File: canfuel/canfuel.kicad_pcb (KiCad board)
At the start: 2 copper layers, 55 x 45 mm, 0 parts

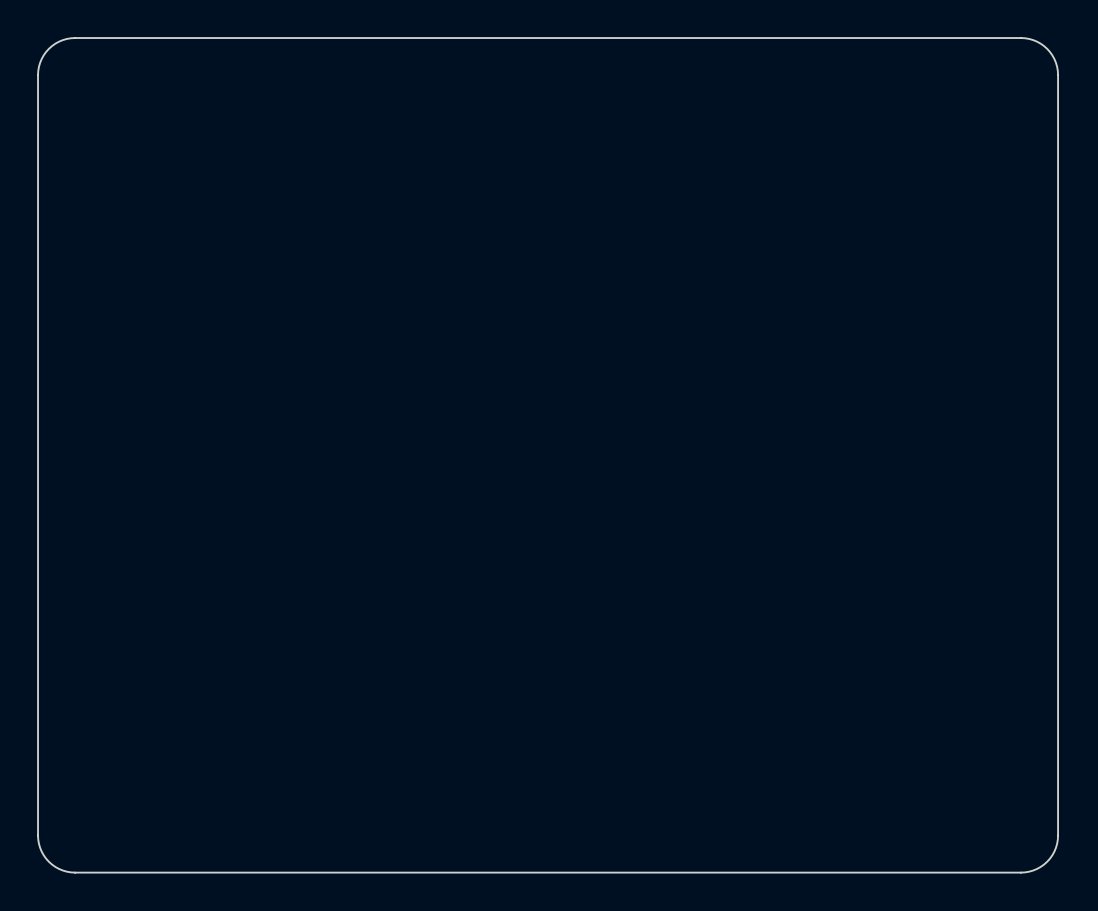
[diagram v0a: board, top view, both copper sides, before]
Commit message: Drop the enclosure and put the mounting holes in
The enclosure has blocked the layout since the project started, on the grounds
that the M3 hole positions were a guess until it was measured and were the one
thing that could force a respin. Closing it by choosing a box turned out to be
the wrong move; closing it by not having one is the right one.

A box was buying nothing here. Everything around the board in the vent is
plastic, so there is no metal to short against. The vent is closed off by a
flap, so there is no airflow, no meaningful dust and no water. The board is
invisible either way. That leaves mechanical retention, and standoffs buy that
better than a box does.

The measurement argued the same way. The space was only ever an estimate - the
MFD15 sits in the way and the depth cannot be measured around it - and the
closest off-the-shelf candidate, a Hammond 1550Q, is 60 x 55 x 30.10 mm against
an estimated 65 x 55 x 30: exactly at the limit on two axes and over on the
third. Its 3 mm die-cast walls would have forced corner notches in the board,
added an isolation and grounding decision that plastic does not, and needed a
slot filed through cast aluminium for the Micro-Fit connectors.

Dropping it inverts the risk. H1-H4 go in at 4 mm from each edge, a 47 x 37 mm
pattern, and because they answer to nothing they stopped being a respin risk
and became cheap insurance: any later mounting scheme is designed around them.
Their references sit on F.Fab rather than F.SilkS, because at 4 mm in from the
edge the silkscreen text overhung the board on the two holes near the top.

Mounting as decided: nylon M3 standoffs, feet on automotive-grade double-sided
tape. Standoffs because the through-hole solder joints must not bear on
anything, VHB-grade tape because a dashboard reaches 50-60 C in summer. Tape
wrapped round the board was considered and rejected - at those temperatures the
adhesive creeps across the board and into the sockets, and it insulates against
metal that 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
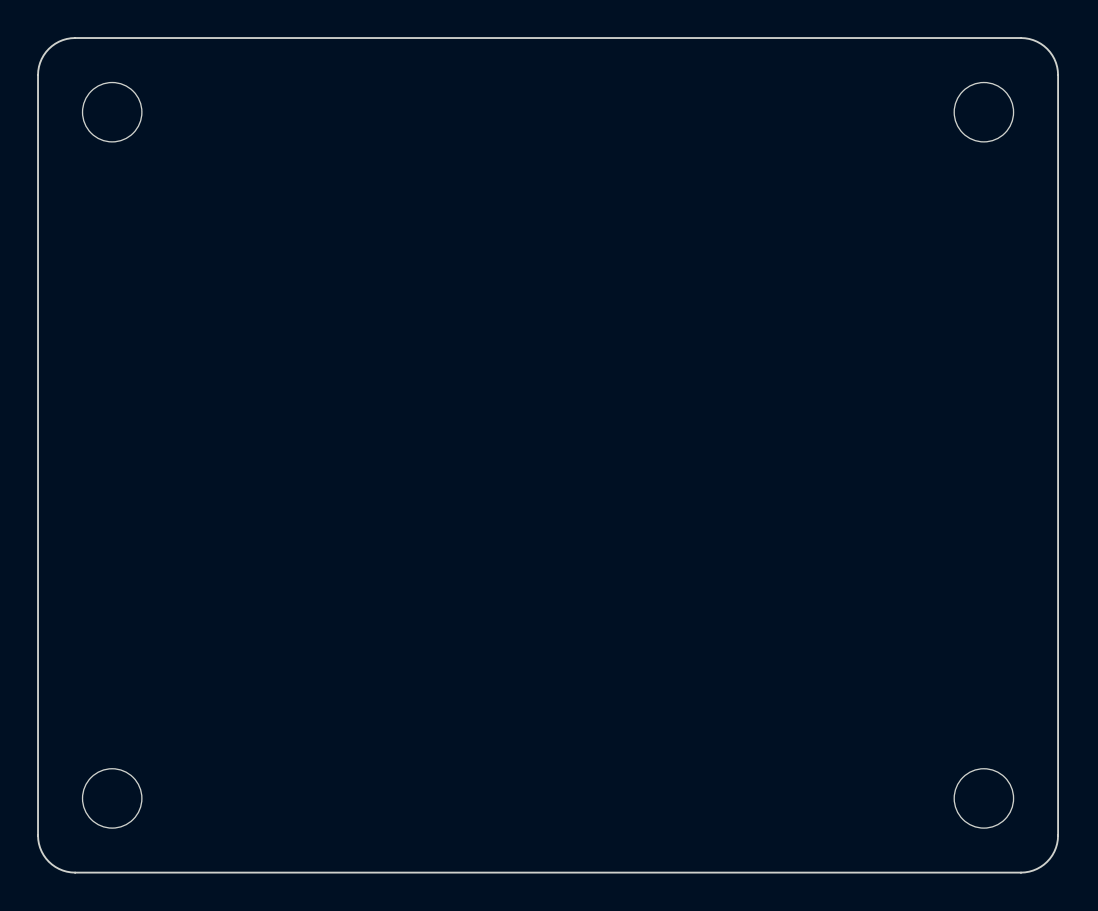
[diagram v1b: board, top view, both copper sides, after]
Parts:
- added H1: MountingHole_3.2mm_M3, MountingHole:MountingHole_3.2mm_M3, F.Cu at (54.0, 54.0)
- added H2: MountingHole_3.2mm_M3, MountingHole:MountingHole_3.2mm_M3, F.Cu at (101.0, 54.0)
- added H3: MountingHole_3.2mm_M3, MountingHole:MountingHole_3.2mm_M3, F.Cu at (54.0, 91.0)
- added H4: MountingHole_3.2mm_M3, MountingHole:MountingHole_3.2mm_M3, F.Cu at (101.0, 91.0)
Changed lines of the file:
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@@
 		(layer "Edge.Cuts")
+	)
+	(footprint "MountingHole:MountingHole_3.2mm_M3"
+		(layer "F.Cu")
+		(at 54 54)
+		(descr "Mounting Hole 3.2mm, M3, no annular")
+		(tags "mountinghole M3")
+		(property "Reference" "H1"
+			(at 0 -4.15 0)
+			(layer "F.Fab")
+			(effects
+				(font
+					(size 1 1)
+					(thickness 0.15)
+				)
+			)
+		)
+		(property "Value" "MountingHole_3.2mm_M3"
+			(at 0 4.15 0)
+			(layer "F.Fab")
+			(hide yes)
+			(effects
+				(font
+					(size 1 1)
+					(thickness 0.15)
+				)
+			)
+		)
+		(attr exclude_from_pos_files exclude_from_bom)
+		(fp_circle
+			(center 0 0)
+			(end 3.2 0)
+			(stroke
+				(width 0.15)
+				(type solid)
+			)
+			(fill no)
+			(layer "Cmts.User")
+		)
+		(fp_circle
+			(center 0 0)
+			(end 3.45 0)
+			(stroke
+				(width 0.05)
+				(type solid)
+			)
+			(fill no)
+			(layer "F.CrtYd")
+		)
+		(pad "" np_thru_hole circle
+			(at 0 0)
+			(size 3.2 3.2)
+			(drill 3.2)
+			(layers "*.Cu" "*.Mask")
+		)
+	)
+	(footprint "MountingHole:MountingHole_3.2mm_M3"
+		(layer "F.Cu")
+		(at 101 54)
+		(descr "Mounting Hole 3.2mm, M3, no annular")
+		(tags "mountinghole M3")
+		(property "Reference" "H2"
+			(at 0 -4.15 0)
+			(layer "F.Fab")
+			(effects
+				(font
+					(size 1 1)
+					(thickness 0.15)
+				)
+			)
+		)
+		(property "Value" "MountingHole_3.2mm_M3"
+			(at 0 4.15 0)
+			(layer "F.Fab")
+			(hide yes)
+			(effects
+				(font
+					(size 1 1)
+					(thickness 0.15)
+				)
+			)
+		)
+		(attr exclude_from_pos_files exclude_from_bom)
+		(fp_circle
+			(center 0 0)
+			(end 3.2 0)
+			(stroke
+				(width 0.15)
+				(type solid)
+			)
+			(fill no)
+			(layer "Cmts.User")
+		)
+		(fp_circle
+			(center 0 0)
+			(end 3.45 0)
+			(stroke
+				(width 0.05)
+				(type solid)
+			)
+			(fill no)
+			(layer "F.CrtYd")
+		)
+		(pad "" np_thru_hole circle
+			(at 0 0)
+			(size 3.2 3.2)
+			(drill 3.2)
+			(layers "*.Cu" "*.Mask")
+		)
+	)
+	(footprint "MountingHole:MountingHole_3.2mm_M3"
+		(layer "F.Cu")
+		(at 54 91)
+		(descr "Mounting Hole 3.2mm, M3, no annular")
+		(tags "mountinghole M3")
+		(property "Reference" "H3"
+			(at 0 -4.15 0)
+			(layer "F.Fab")
+			(effects
+				(font
+					(size 1 1)
+					(thickness 0.15)
+				)
+			)
+		)
+		(property "Value" "MountingHole_3.2mm_M3"
+			(at 0 4.15 0)
+			(layer "F.Fab")
+			(hide yes)
+			(effects
+				(font
+					(size 1 1)
+					(thickness 0.15)
+				)
+			)
+		)
+		(attr exclude_from_pos_files exclude_from_bom)
+		(fp_circle
+			(center 0 0)
+			(end 3.2 0)
+			(stroke
+				(width 0.15)
+				(type solid)
+			)
+			(fill no)
+			(layer "Cmts.User")
+		)
+		(fp_circle
+			(center 0 0)
+			(end 3.45 0)
+			(stroke
+				(width 0.05)
+				(type solid)
+			)
+			(fill no)
+			(layer "F.CrtYd")
+		)
+		(pad "" np_thru_hole circle
+			(at 0 0)
+			(size 3.2 3.2)
+			(drill 3.2)
+			(layers "*.Cu" "*.Mask")
+		)
+	)
+	(footprint "MountingHole:MountingHole_3.2mm_M3"
+		(layer "F.Cu")
+		(at 101 91)
+		(descr "Mounting Hole 3.2mm, M3, no annular")
+		(tags "mountinghole M3")
+		(property "Reference" "H4"
+			(at 0 -4.15 0)
+			(layer "F.Fab")
+			(effects
+				(font
+					(size 1 1)
+					(thickness 0.15)
+				)
+			)
+		)
+		(property "Value" "MountingHole_3.2mm_M3"
+			(at 0 4.15 0)
+			(layer "F.Fab")
+			(hide yes)
+			(effects
+				(font
+					(size 1 1)
+					(thickness 0.15)
+				)
+			)
+		)
+		(attr exclude_from_pos_files exclude_from_bom)
+		(fp_circle
+			(center 0 0)
+			(end 3.2 0)
+			(stroke
+				(width 0.15)
+				(type solid)
+			)
+			(fill no)
+			(layer "Cmts.User")
+		)
+		(fp_circle
+			(center 0 0)
+			(end 3.45 0)
+			(stroke
+				(width 0.05)
+				(type solid)
+			)
+			(fill no)
+			(layer "F.CrtYd")
+		)
+		(pad "" np_thru_hole circle
+			(at 0 0)
+			(size 3.2 3.2)
+			(drill 3.2)
+			(layers "*.Cu" "*.Mask")
+		)
 	)
 	(embedded_fonts no)

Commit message: Place canfuel PCB parts
Net classes, all 25 footprints, and a silkscreen that can be read. Nothing is
routed yet; DRC is clean and the 70 unconnected items are the ratsnest.

The MCLR network cannot meet DS39977C 2.3 in full. Four parts totalling 71 mm2
of courtyard do not fit in the ~85 mm2 of free area around a corner pin of a
DIP-28, whatever footprints are chosen. R6, the series resistor in the reset
path, is inside the 6 mm circle entirely; C8 and JP2 sit 4.31 and 2.04 mm away
at their near edges; R1, the static pull-up, is the one pushed out. Those
figures are recorded in ALLOW in tools/check-placement.py with their reasons.

R1-R6 became upright P2.54mm parts and C8 a 2.50 mm disc. That is how the
maintainer fits axial resistors anyway, and it is the only reason R6 fits at
all: 3.95 mm reach standing against 11.36 mm lying down.

C7 is turned across U1 rather than along it. Lying along the pin row its ground
pad shorted pin 5; in the channel between the rows it clears both by 0.79 mm
and still lands 2.25 mm from pin 6.

Two new tools, because neither DRC nor kicad-cli covers this ground:

  check-placement.py   measures the four datasheet distance rules and the
                       mounting-hole keepouts. DRC will happily pass a board
                       with a decoupling capacitor 40 mm from its pin.
  import-footprints.py Update PCB from Schematic without the GUI; kicad-cli
                       has no equivalent. Safe to re-run - placement survives.

Also corrects the CLAUDE.md note claiming permissions use defaultMode dontAsk.
They do not, and should not: dontAsk does not widen the allow list, so unmatched
commands are silently rejected instead of prompting.

Co-Authored-By: Claude Opus 5 <noreply@anthropic.com>
Claude-Session: https://claude.ai/code/session_01UuRx2iytAQXHULyNP41hBq
@
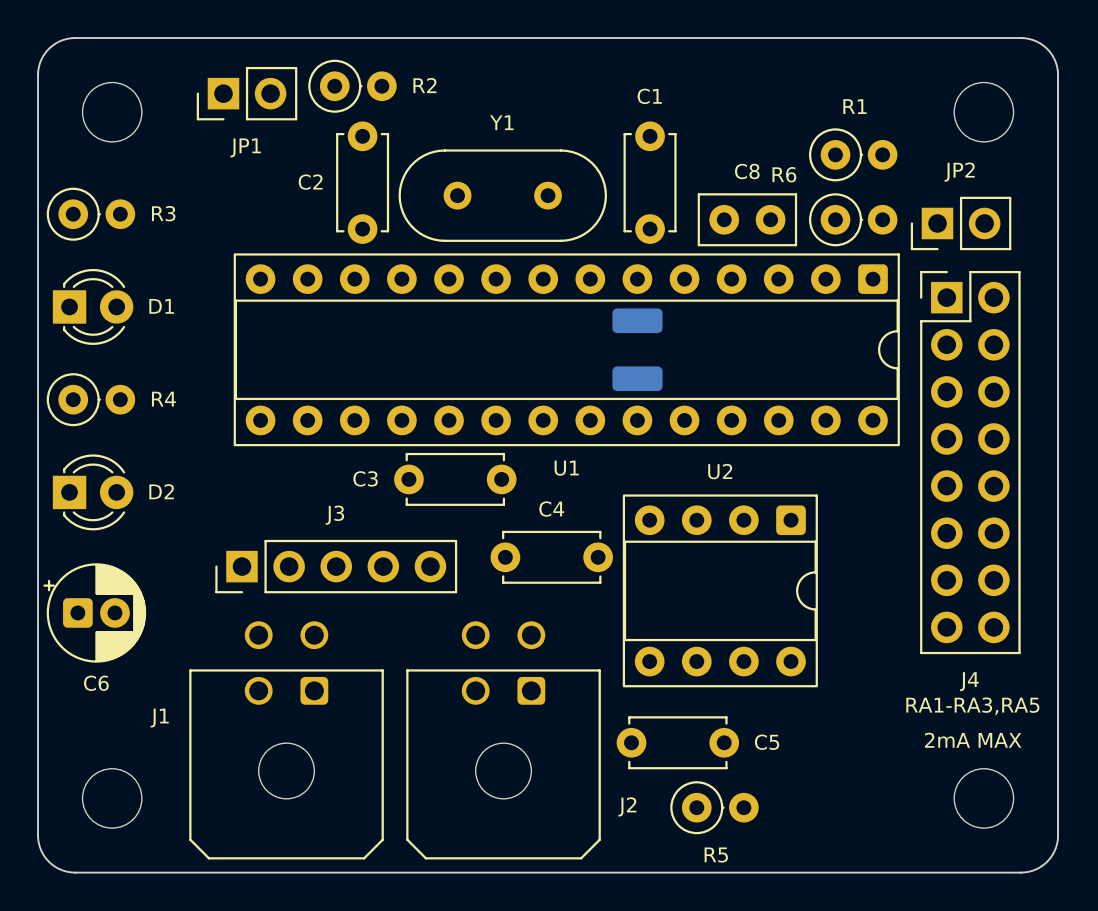
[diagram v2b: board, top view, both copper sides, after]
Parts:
- added C1: 33p, Capacitor_THT:C_Disc_D5.0mm_W2.5mm_P5.00mm, F.Cu at (83.0, 60.3)
- added C2: 33p, Capacitor_THT:C_Disc_D5.0mm_W2.5mm_P5.00mm, F.Cu at (67.5, 60.3)
- added C3: 100n, Capacitor_THT:C_Disc_D5.0mm_W2.5mm_P5.00mm, F.Cu at (70.0, 73.8)
- added C4: 100n, Capacitor_THT:C_Disc_D5.0mm_W2.5mm_P5.00mm, F.Cu at (80.2, 78.0)
- added C5: 100n, Capacitor_THT:C_Disc_D5.0mm_W2.5mm_P5.00mm, F.Cu at (82.0, 88.0)
- added C6: 10u, Capacitor_THT:CP_Radial_D5.0mm_P2.00mm, F.Cu at (52.1, 81.0)
- added C7: 10u, Capacitor_SMD:C_1210_3225Metric_Pad1.33x2.70mm_HandSolder, B.Cu at (82.3, 66.8)
- added C8: 100n, Capacitor_THT:C_Disc_D5.0mm_W2.5mm_P2.50mm, F.Cu at (87.0, 59.8)
- added D1: green, LED_THT:LED_D3.0mm, F.Cu at (51.7, 64.5)
- added D2: yellow, LED_THT:LED_D3.0mm, F.Cu at (51.7, 74.5)
- added J1: Micro-Fit 43045-0400, Connector_Molex:Molex_Micro-Fit_3.0_43045-0400_2x02_P3.00mm_Horizontal, F.Cu at (64.9, 85.2)
- added J2: Micro-Fit 43045-0400, Connector_Molex:Molex_Micro-Fit_3.0_43045-0400_2x02_P3.00mm_Horizontal, F.Cu at (76.6, 85.2)
- added J3: ICSP, Connector_PinHeader_2.54mm:PinHeader_1x05_P2.54mm_Vertical, F.Cu at (61.0, 78.5)
- added J4: ESCAPE, Connector_PinHeader_2.54mm:PinHeader_2x08_P2.54mm_Vertical, F.Cu at (99.0, 64.0)
- added JP1: DBG, Connector_PinHeader_2.54mm:PinHeader_1x02_P2.54mm_Vertical, F.Cu at (60.0, 53.0)
- added JP2: MCLR, Connector_PinHeader_2.54mm:PinHeader_1x02_P2.54mm_Vertical, F.Cu at (98.5, 60.0)
- added R1: 10k, Resistor_THT:R_Axial_DIN0207_L6.3mm_D2.5mm_P2.54mm_Vertical, F.Cu at (93.0, 56.3)
- added R2: 10k, Resistor_THT:R_Axial_DIN0207_L6.3mm_D2.5mm_P2.54mm_Vertical, F.Cu at (66.0, 52.6)
- added R3: 1k, Resistor_THT:R_Axial_DIN0207_L6.3mm_D2.5mm_P2.54mm_Vertical, F.Cu at (51.9, 59.5)
- added R4: 1k, Resistor_THT:R_Axial_DIN0207_L6.3mm_D2.5mm_P2.54mm_Vertical, F.Cu at (51.9, 69.5)
- added R5: 120R, Resistor_THT:R_Axial_DIN0207_L6.3mm_D2.5mm_P2.54mm_Vertical, F.Cu at (85.5, 91.5)
- added R6: 470R, Resistor_THT:R_Axial_DIN0207_L6.3mm_D2.5mm_P2.54mm_Vertical, F.Cu at (93.0, 59.8)
- added U1: PIC18F25K80, Package_DIP:DIP-28_W7.62mm_Socket, F.Cu at (95.0, 63.0)
- added U2: MCP2562-E/P, Package_DIP:DIP-8_W7.62mm_Socket, F.Cu at (90.6, 76.0)
- added Y1: 16MHz, Crystal:Crystal_HC49-U_Vertical, F.Cu at (77.5, 58.5)
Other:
- board text added: "2mA MAX"
- board text added: "RA1-RA3,RA5"

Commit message: Route canfuel PCB, and drop the escape header
DRC is clean with zero unconnected items. Two layers, SGND poured on both,
thermal reliefs on every pad because the board is hand soldered.

J4 is gone, and it went on measurement rather than argument. Routing the same
placement with the same router, with and without it:

                        with J4   without J4
  connections               39           25
  left unroutable            8            0
  DRC                incomplete   0 violations

Five of those eight failures were not escape signals: both status LEDs and the
whole ICSP header. J4's fourteen signals congest the channel between U1's pin
rows, which is the only way across a 55 x 45 mm board, and ICSP is what
starves. A header that exists to rescue a design error was stopping the chip
being programmed. Patching now goes onto the PDIP socket pins from underneath,
which was always the real escape hatch.

U1's fourteen unused pins carry no-connect flags. check-netlist.py grew an NC
sentinel for them rather than transcribing the generated net names.

The freed column turned out to sit inside the 6 mm circle DS39977C 2.3 draws
around pin 1, which is why the MCLR cluster could never be tightened before.
Re-placed by search: worst far corner 10.68 -> 8.67 mm, and all four parts now
within 2.5 mm of the pin at their nearest edge. The earlier arrangement had R6
wholly inside but left C8 - the reset capacitor, the part the section's own
Figure 2-2 note is about - furthest away.

check-placement.py now also asserts what 2.6 says about copper: no signal or
power traces inside the oscillator guard, nothing at all on B.Cu under the
crystal. Both are given to the router as keep-outs and re-checked afterwards,
so they cannot quietly rot.

Two things the routing taught, recorded in plan 5.3:

  Net order decides whether it finishes. Oscillator and VCAP first then the
  rest alphabetically managed 32 of 39; longest-first managed 25 and +5V-last
  managed 27. The 0.8 mm +5V 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
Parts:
- removed J4: ESCAPE, Connector_PinHeader_2.54mm:PinHeader_2x08_P2.54mm_Vertical
- moved C8 8.42 mm to (95.4, 59.8), turned to 90 degrees
- moved R6 6.23 mm to (99.0, 61.4), turned to 90 degrees
- moved JP2 5.40 mm to (98.6, 65.4), turned to 0 degrees
- moved R1 4.47 mm to (90.2, 59.8)
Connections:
- U1 pad 13: ESC_RC2 -> unconnected-(U1-CCP2/RC2-Pad13)
- U1 pad 14: ESC_RC3 -> unconnected-(U1-SCL/SCK/RC3-Pad14)
- U1 pad 15: ESC_RC4 -> unconnected-(U1-SDA/SDI/RC4-Pad15)
- U1 pad 16: ESC_RC5 -> unconnected-(U1-SDO/RC5-Pad16)
- U1 pad 17: CANTX2 -> unconnected-(U1-CANTX/TX1/CCP3/RC6-Pad17)
- U1 pad 18: CANRX2 -> unconnected-(U1-CANRX/RX1/CCP4/RC7-Pad18)
- U1 pad 21: ESC_RB0 -> unconnected-(U1-AN10/INT0/RB0-Pad21)
- U1 pad 22: ESC_RB1 -> unconnected-(U1-AN8/INT1/RB1-Pad22)
- U1 pad 25: ESC_RB4 -> unconnected-(U1-AN9/ECCP1/RB4-Pad25)
- U1 pad 26: ESC_RB5 -> unconnected-(U1-CCP5/RB5-Pad26)
- U1 pad 3: ESC_RA1 -> unconnected-(U1-RA1/AN1-Pad3)
- U1 pad 4: ESC_RA2 -> unconnected-(U1-RA2/Vref-/AN2-Pad4)
- U1 pad 5: ESC_RA3 -> unconnected-(U1-RA3/Vref+/AN3-Pad5)
- U1 pad 7: ESC_RA5 -> unconnected-(U1-RA5/AN4-Pad7)
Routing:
- net +5V: track 0.00 -> 164.8 mm
- net ~{MCLR}: track 0.00 -> 93.0 mm, vias 0 -> 1
- net DBG_EN: track 0.00 -> 44.2 mm
- net CANL: track 0.00 -> 35.9 mm
- net CANH: track 0.00 -> 33.9 mm
- net PGD: track 0.00 -> 32.9 mm, vias 0 -> 1
- net PGC: track 0.00 -> 30.6 mm
- net LED_PWR: track 0.00 -> 27.3 mm, vias 0 -> 3
- net LED_CAN: track 0.00 -> 18.8 mm, vias 0 -> 1
- net MCLR_RC: track 0.00 -> 17.3 mm
- net OSC1: track 0.00 -> 11.9 mm
- net OSC2: track 0.00 -> 10.5 mm
- net CAN_TX: track 0.00 -> 10.4 mm
- net MCLR_C: track 0.00 -> 9.53 mm
- net CAN_RX: track 0.00 -> 6.15 mm
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- added copper zone on B.Cu, net SGND
- added copper zone on F.Cu, net SGND
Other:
- board text removed: "2mA MAX"
- board text removed: "RA1-RA3,RA5"
